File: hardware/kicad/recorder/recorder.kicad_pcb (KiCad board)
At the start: 4 copper layers, 64 x 86 mm, 60 parts, among them J1 UART0, J2 USB_C_16P, J3 microSD, SW1 record, U1 ESP32-S3-MINI-1U-N8, U2 ES8311, U3 MCP73831-2-OT, U4 AP2112K-3.3, U5 AP22804AW5, U6 NS4150B, U7 USBLC6-2SC6, U8 LP5907MFX-3.3, Y1 12.288MHz

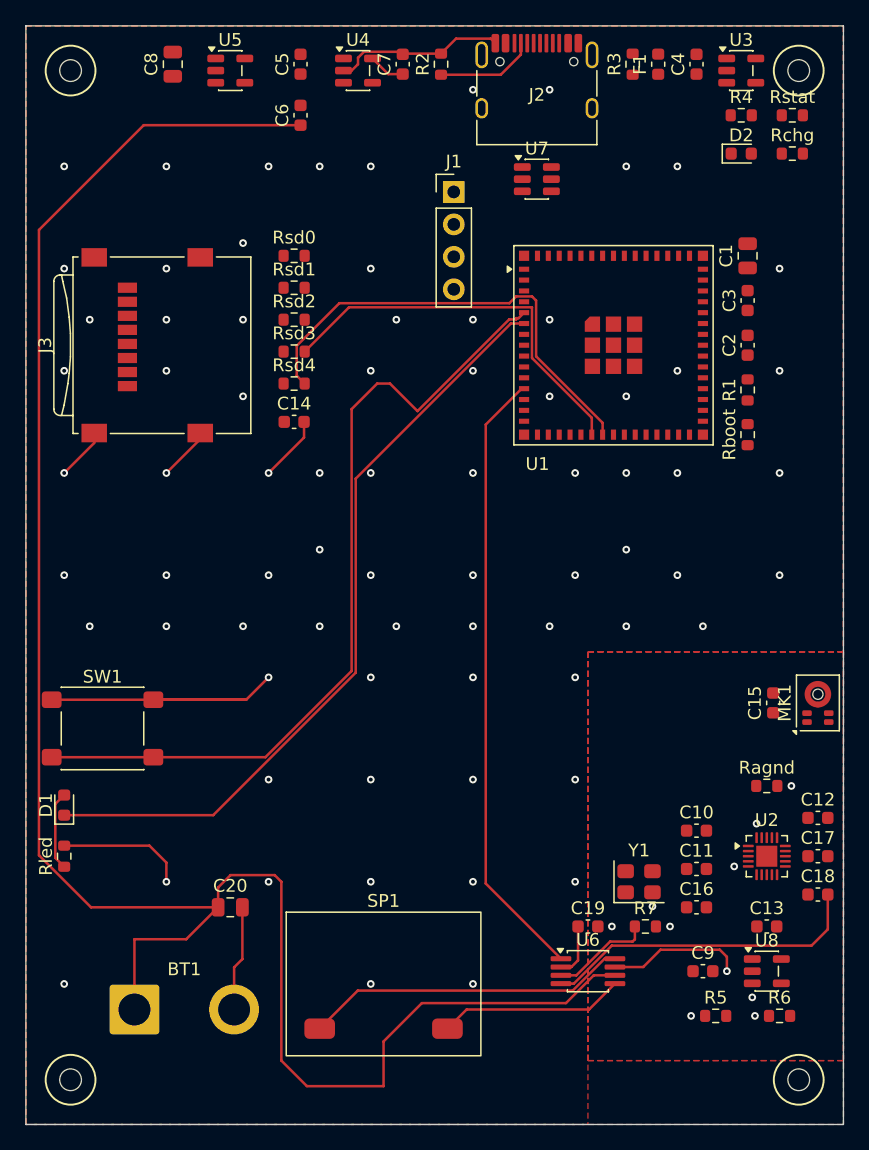
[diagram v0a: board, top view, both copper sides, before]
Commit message: Route the recorder board and make the fab package match it
The board had planes but no signals. It now carries 694 traces and 193
vias from freerouting, driven headless through Specctra DSN/SES, with the
USB pair, the ES8311 fanout and the analog island hand-routed first and
locked so rip-up cannot cut them.

kicad-cli pcb drc now reports zero violations at every severity and zero
unconnected items.

Two things that would have scrapped a real order:

- check_gates.py re-exported Gerbers but left the drill file, the
  pick-and-place CSV and recorder-jlc.zip at whatever date they were
  committed with. The drill file on disk predated routing and had no
  0.3 mm tool, so the package described a board with none of its vias
  drilled. The whole package is now written in one pass from one board
  file, gated on a real kicad-cli pcb drc run.
- check_placement.py trusted BOX2I.Merge()'s return value, which is an
  unrelated proxy in the SWIG bindings, and measured courtyards from
  GetCourtyard(), which is inflated past the drawn outline. That invented
  four off-board mounting holes and six overlaps. It reads the drawn
  shapes now, and check_gates runs it when pcbnew is importable.

Silkscreen designators are shrunk to the 0.8 mm / 0.15 mm fab floor and
re-seated on a full angular sweep, clearing all 29 silk warnings.

Co-authored-by: zeeman <zeeman-effect@users.noreply.github.com>
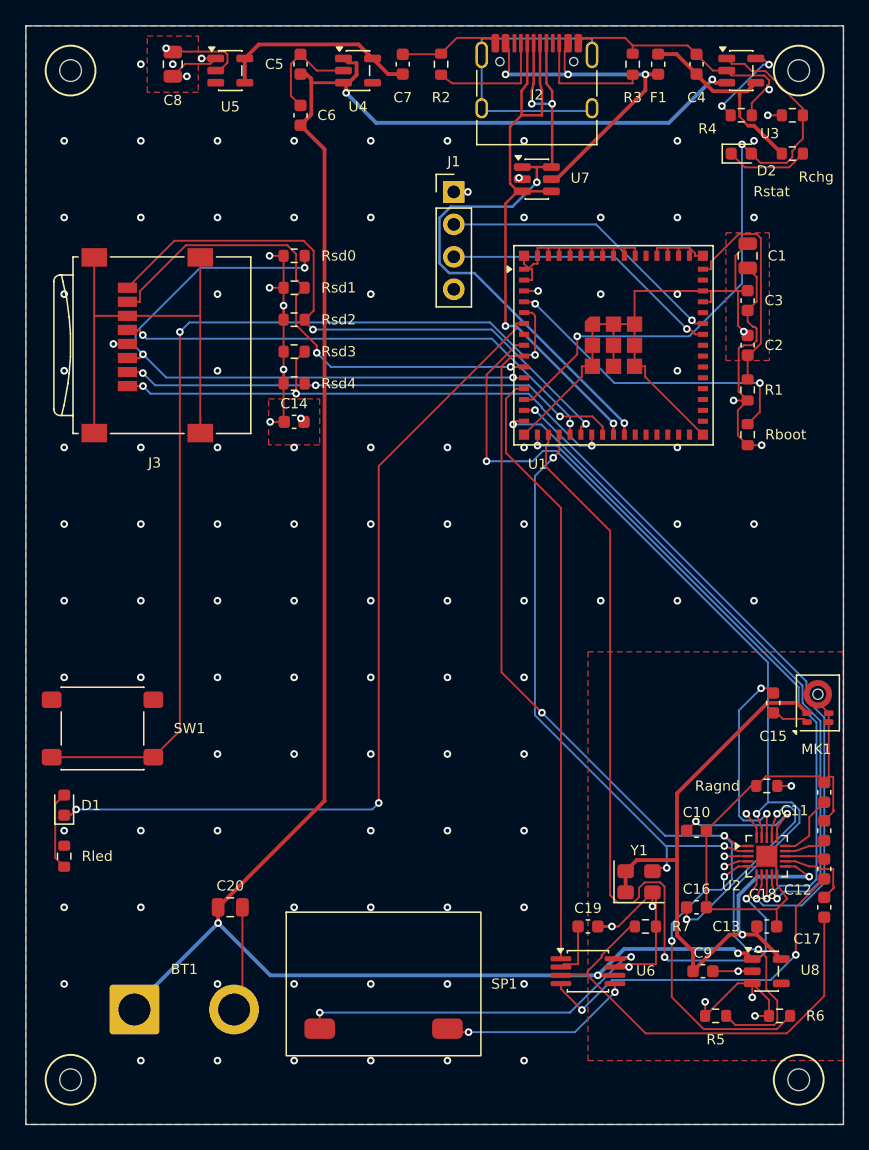
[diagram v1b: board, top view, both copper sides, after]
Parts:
- MK1: footprint Infineon_PG-LLGA-5-2 -> IM73A135_PG-LLGA-5-3
- U1: footprint ESP32-S2-MINI-1U -> ESP32-S3-MINI-1U
- moved C11 11.7 mm to (30.5, 17.0), turned to 90 degrees
- moved C17 4.03 mm to (30.5, 26.0), turned to -90 degrees
- moved C18 2.06 mm to (30.5, 23.0), turned to -90 degrees
- moved C12 1.12 mm to (30.5, 20.0), turned to 90 degrees
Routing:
- net GND: track 81.0 -> 187.6 mm, vias 53 -> 101
- net I2C_SDA: track 0.00 -> 81.8 mm, vias 0 -> 3
- net I2C_SCL: track 0.00 -> 77.2 mm, vias 0 -> 3
- net VDD33: track 0.00 -> 65.2 mm, vias 31 -> 20
- net I2S_BCLK: track 0.00 -> 64.7 mm, vias 0 -> 2
- net I2S_DIN: track 0.00 -> 55.4 mm, vias 0 -> 2
- net 3V3A: track 0.00 -> 54.9 mm, vias 0 -> 2
- net I2S_DOUT: track 0.00 -> 53.9 mm, vias 0 -> 2
- net USB_DP: track 0.00 -> 52.6 mm, vias 0 -> 4
- net I2S_WS: track 0.00 -> 51.1 mm, vias 0 -> 2
- net SD_CMD: track 0.00 -> 50.2 mm, vias 0 -> 3
- net CHG_STAT: track 0.00 -> 49.0 mm, vias 0 -> 2
- net SD_D1: track 0.00 -> 48.7 mm, vias 0 -> 2
- net I2S_MCLK: track 0.00 -> 46.7 mm, vias 0 -> 3
- net USB_DM: track 0.00 -> 45.7 mm, vias 0 -> 2
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- removed copper zone on F.Cu, net 3V3A

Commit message: Route USB as a real pair and ground the USB-C shell
The autorouter sent D+ on a 16.6 mm diagonal across B.Cu. B.Cu is the face
that lies against the phone and is otherwise a solid GND pour, so that
slotted the shield and ran a USB line straight at the handset.

U1's USB pads sit on the module's top row, the far side of a 15.9 mm
module from J2, and the castellations leave 0.05 mm between pads, so the
pair cannot cross the footprint. It now goes up the 3.3 mm channel
between J1 and U1 in two lanes 0.4 mm apart. Both nets already surface
west of J2 on their own link, so extending those links west drops each
into its lane with no crossing anywhere on the board. U7 hangs off the
lanes as a short stub instead of sitting in series, which costs nothing:
it is a shunt TVS and clamps to GND wherever it is tapped.

D+ 45.8 mm, D- 44.2 mm end to end. Skew is down from 6.9 mm to 1.65 mm
and B.Cu on the pair from 30 mm to 4.4 mm.

J2's shell was a no-connect, which left the four retention tabs on a
placeholder net that DRC wanted joined to each other and no amount of
re-routing could close. It is GND now, which is what a connector shell
wants anyway.

generate_recorder.py assumed the Windows KiCad install path, so it only
ran on one laptop; it searches the usual locations now.

Co-authored-by: zeeman <zeeman-effect@users.noreply.github.com>
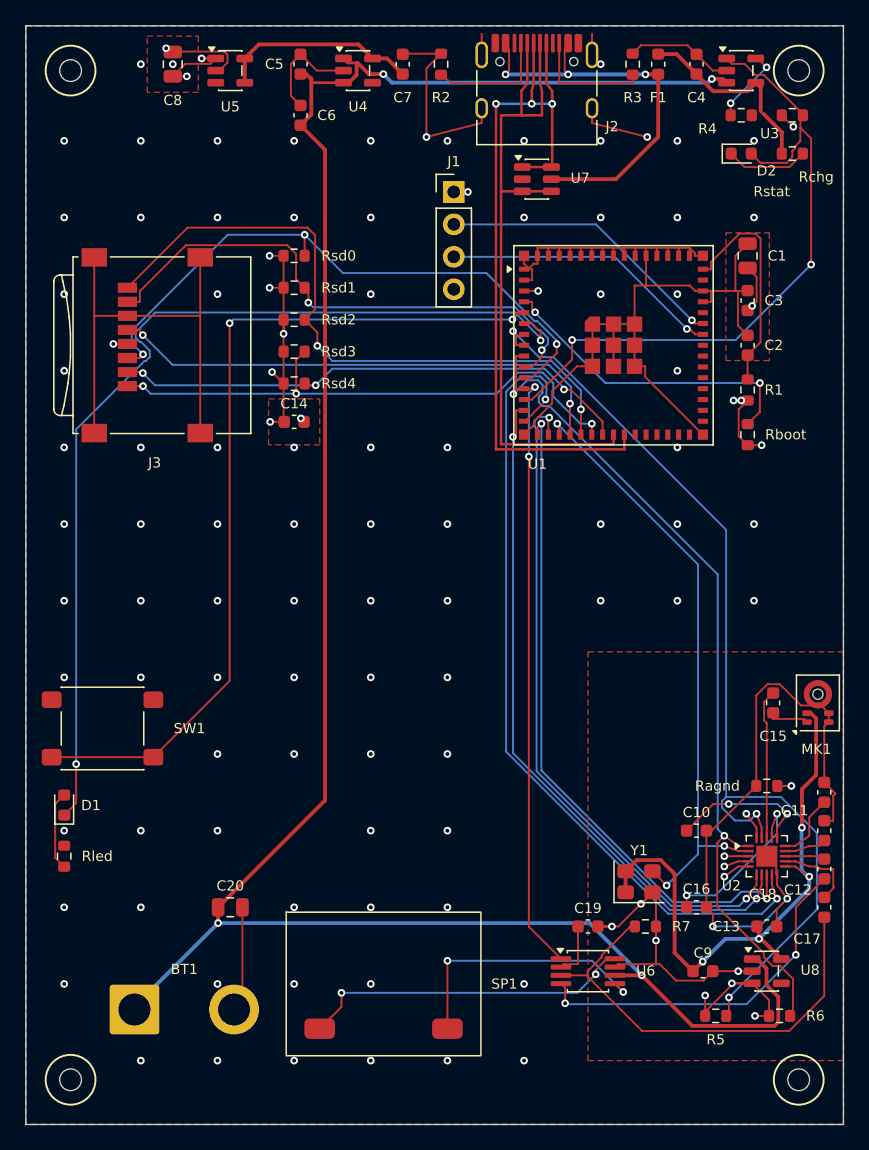
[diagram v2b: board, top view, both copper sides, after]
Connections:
- J2 pad SH: unconnected-(J2-SHIELD-PadSH) -> GND
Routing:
- net unconnected-(J2-SHIELD-PadSH): track 24.2 -> 0.00 mm
- net GND: track 187.6 -> 203.2 mm, vias 101 -> 94
- net I2S_BCLK: track 64.7 -> 53.3 mm
- net I2S_DOUT: track 53.9 -> 64.7 mm
- net /Audio/AGND: track 40.0 -> 50.0 mm, vias 0 -> 2
- net I2C_SCL: track 77.2 -> 67.7 mm, vias 3 -> 2
- net LED: track 67.6 -> 76.7 mm
- net USB_DM: track 45.7 -> 53.9 mm, vias 2 -> 0
- net 3V3A: track 54.9 -> 46.8 mm, vias 2 -> 4
- net BTN: track 75.3 -> 68.0 mm
- net VDD33: track 65.2 -> 57.9 mm, vias 20 -> 22
- net USB_DP: track 52.6 -> 59.6 mm, vias 4 -> 3
- net VBAT: track 166.2 -> 172.4 mm, vias 5 -> 4
- net /Audio/SPK_N: track 15.2 -> 21.0 mm
- net CHG_STAT: track 49.0 -> 54.0 mm
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
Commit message: Rebuild the board and the fab package against the tightened rules
Applies the rule, footprint and parity changes to recorder.kicad_pcb:
silk re-seated at 1.0 mm, pours backed off the mounting-hole barrels to
0.3 mm, MK1's ring pad opened up, library-qualified footprint names, and
two redundant vias dropped next to J1 and J2 pads. 695 tracks, 185 vias,
8 zones.

kicad-cli pcb drc: 0 violations at every severity, 0 unconnected. The 27
remaining --schematic-parity notes are all expected and now recorded in
placement.json: 22 module pads with no schematic pin (spare ESP32-S3 GPIO
castellations, NC pins, the USB-C SBU pair), the 4 mounting holes, which
are mechanical and have no symbol, and SP1's Description field.

Gerbers, both drill files, the pick-and-place CSV and recorder-jlc.zip
re-exported from this board in one pass.

Co-authored-by: zeeman <zeeman-effect@users.noreply.github.com>
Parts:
- BT1: footprint SolderWire-2sqmm_1x02_P7.8mm_D2mm_OD3.9mm -> Connector_Wire:SolderWire-2sqmm_1x02_P7.8mm_D2mm_OD3.9mm
- C1, C20, C8: footprint C_0805_2012Metric -> Capacitor_SMD:C_0805_2012Metric
- C10, C11, C12, C13, C14, C15, C16, C17, C18, C19, C2, C3, C4, C5, C6, C7, C9: footprint C_0603_1608Metric -> Capacitor_SMD:C_0603_1608Metric
- D1, D2: footprint LED_0603_1608Metric -> LED_SMD:LED_0603_1608Metric
- F1: footprint Fuse_0603_1608Metric -> Fuse:Fuse_0603_1608Metric
- H1, H2, H3, H4: footprint MountingHole_1.7mm_M1.6 -> PSV:MountingHole_1.7mm_M1.6
- J1: footprint PinHeader_1x04_P2.54mm_Vertical -> Connector_PinHeader_2.54mm:PinHeader_1x04_P2.54mm_Vertical
- J2: footprint USB_C_Receptacle_HRO_TYPE-C-31-M-12 -> Connector_USB:USB_C_Receptacle_HRO_TYPE-C-31-M-12
- J3: footprint microSD_HC_Wuerth_693072010801 -> Connector_Card:microSD_HC_Wuerth_693072010801
- MK1: footprint IM73A135_PG-LLGA-5-3 -> PSV:IM73A135_PG-LLGA-5-3
- R1, R2, R3, R4, R5, R6, R7, Ragnd, Rboot, Rchg, Rled, Rsd0, Rsd1, Rsd2, Rsd3, Rsd4, Rstat: footprint R_0603_1608Metric -> Resistor_SMD:R_0603_1608Metric
- SP1: footprint Speaker_15x11mm -> PSV:Speaker_15x11mm
- SW1: footprint SW_SPST_PTS645Sx43SMTR92 -> Button_Switch_SMD:SW_SPST_PTS645Sx43SMTR92
- U1: footprint ESP32-S3-MINI-1U -> PSV:ESP32-S3-MINI-1U
- U2: footprint QFN-20-1EP_3x3mm_P0.4mm_EP1.65x1.65mm -> Package_DFN_QFN:QFN-20-1EP_3x3mm_P0.4mm_EP1.65x1.65mm
- U3, U4, U5, U8: footprint SOT-23-5 -> Package_TO_SOT_SMD:SOT-23-5
- U6: footprint MSOP-8_3x3mm_P0.65mm -> Package_SO:MSOP-8_3x3mm_P0.65mm
- U7: footprint SOT-23-6 -> Package_TO_SOT_SMD:SOT-23-6
- Y1: footprint Oscillator_SMD_Abracon_ASE-4Pin_3.2x2.5mm -> Oscillator:Oscillator_SMD_Abracon_ASE-4Pin_3.2x2.5mm
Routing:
- net VDD33: track 57.9 -> 56.8 mm, vias 22 -> 21
- net GND: vias 94 -> 93

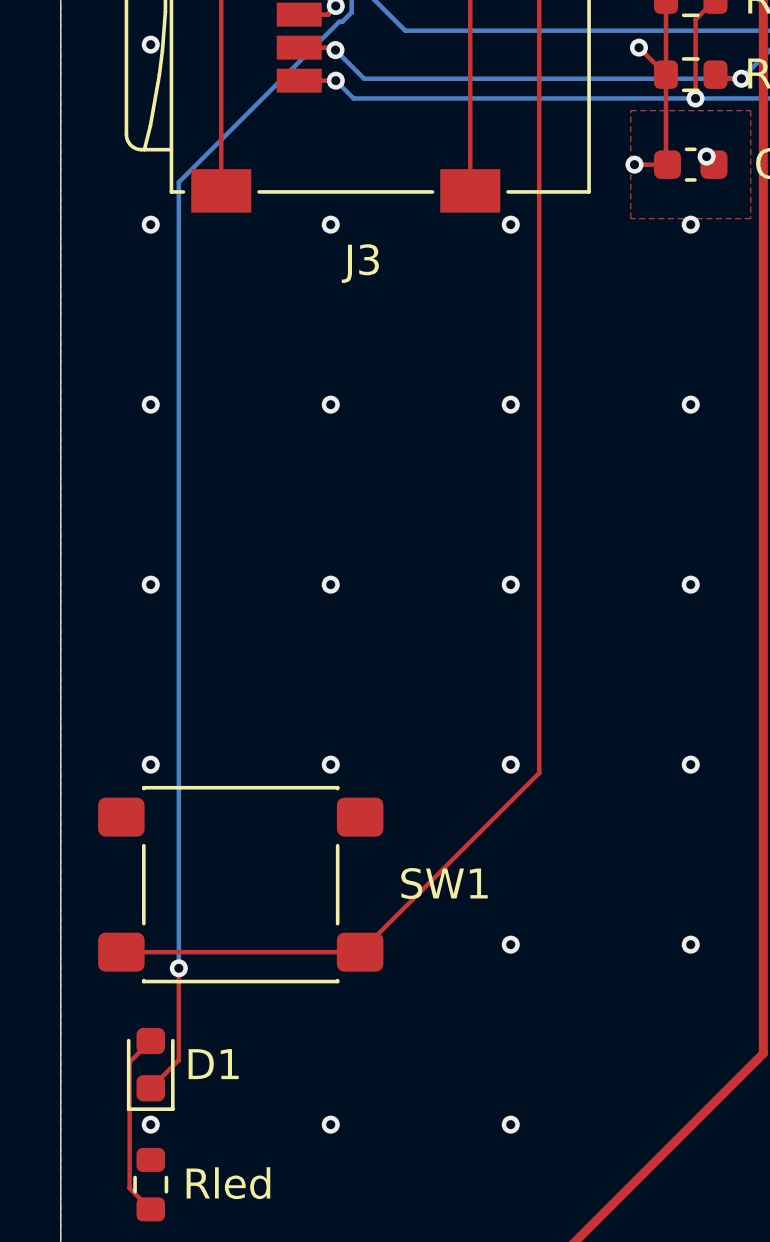
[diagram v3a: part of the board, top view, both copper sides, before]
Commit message: Swap SW1 for a side-actuated switch so the case needs no lever
The record button is on the left long wall, but SW1 was a top-actuated
PTS645: the plunger pointed at the phone, not at the wall. Every version of
that ends in a moulded lever inside a 9 mm stack, pivoting a sideways press
into a downward one, with the travel budget of a 3D print.

Panasonic EVQP7C01P instead. Side push, SPST, 3.5 x 2.9 x 1.35 mm, 2.2 N,
0.2 mm travel, reflow, JLCPCB C388883 and in stock. KiCad 10 already ships
the land as Button_Switch_SMD:SW_SPST_EVQP7C, and its two moulded bosses
drop into 0.7 mm NPTH holes that take the sideways load instead of the
solder joints. Rotated 270 and pushed out to x = -29.3, the actuator tip
stops 0.6 mm inside the board edge with copper still 1.46 mm off the cut.

Pin 1 now carries BTN and pin 2 GND, the other way round from the old part.
A push button's terminals are interchangeable, and after the rotation pin 2
is the pad row nearest the edge, where the F.Cu GND pour reaches it with no
trace at all; BTN gets the inner row, which has room to leave the part. The
LED via moved up to (-27.30, 16.00) and its B.Cu descent shifted to
x = -27.30 to clear the new footprint and its guide holes.

The case aperture was 7.0 x 3.5 mm, sized for "whatever mechanism this ends
up needing". It is now a 3.0 x 2.2 mm press-through slot over a 1.7 mm
actuator. The case still owes a short moulded nub to span the 0.9 mm from
the inner wall face to the actuator tip.

docs/bom.md called SW1 "side-fire, C318885". C318885 is an XKB
TS-1187A-C-J-B, a 5.1 x 5.1 x 5 mm top-actuated switch, so that line was
wrong about the part and about the direction it fires.

Board re-verified: kicad-cli pcb drc reports 0 violations at every severity,
0 unconnected items and the same 27 expected schematic-parity notes.

Co-authored-by: zeeman <zeeman-effect@users.noreply.github.com>
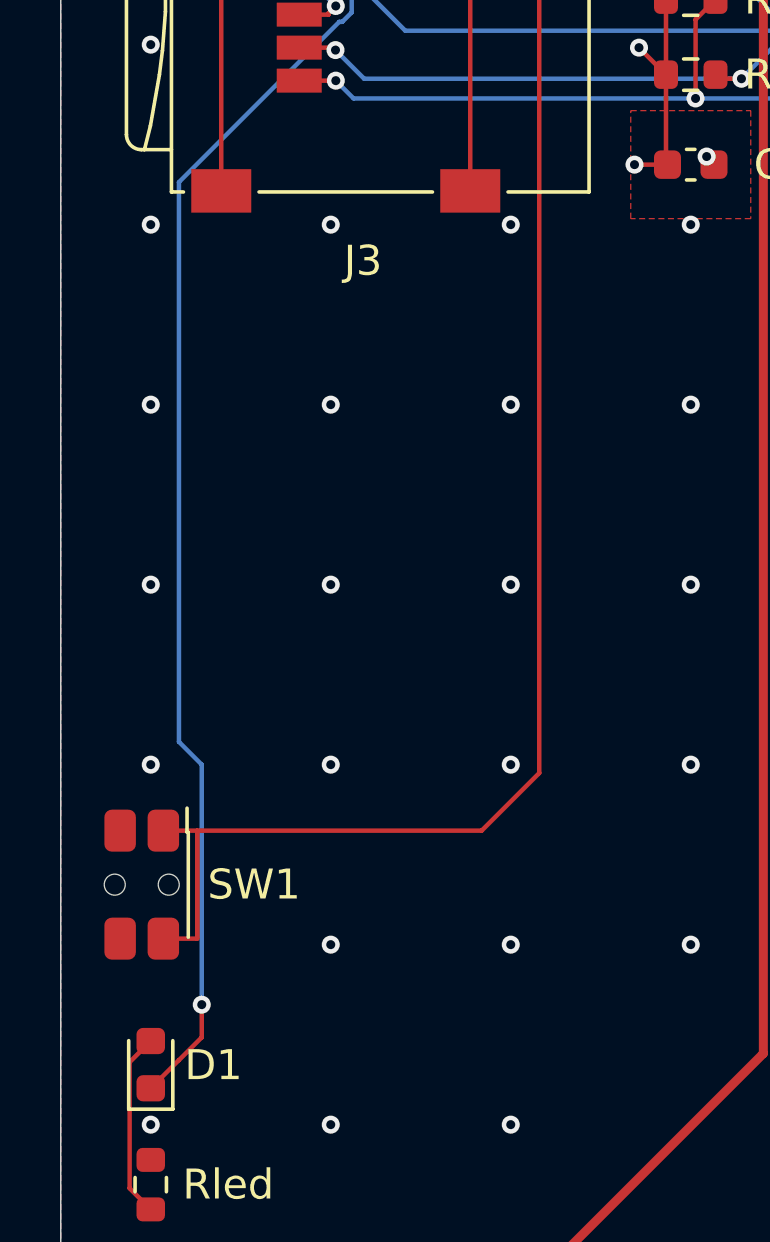
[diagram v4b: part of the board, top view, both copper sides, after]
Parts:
- SW1: footprint Button_Switch_SMD:SW_SPST_PTS645Sx43SMTR92 -> Button_Switch_SMD:SW_SPST_EVQP7C
- moved SW1 3.30 mm to (-29.3, 12.0), turned to -90 degrees
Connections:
- SW1 pad 1: GND -> BTN
- SW1 pad 2: BTN -> GND
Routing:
- net BTN: track 68.0 -> 69.6 mm
- net LED: track 76.7 -> 77.4 mm
- net GND: vias 93 -> 94
